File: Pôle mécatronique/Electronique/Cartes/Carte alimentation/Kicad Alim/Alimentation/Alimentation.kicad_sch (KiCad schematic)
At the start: 16 parts, among them J1 Conn_01x04, J2 Conn_01x04, J3 Conn_01x04, J4 Conn_01x05, J5 Conn_01x05, J6 Conn_02x03_Odd_Even, J7 Conn_02x10_Odd_Even, J8 Conn_01x02, J9 Conn_01x02, K1 G5LE-1, Q1 BD135, U1 TSR_2-2450, U2 TSR_2-2450, U3 TSR_2-24120

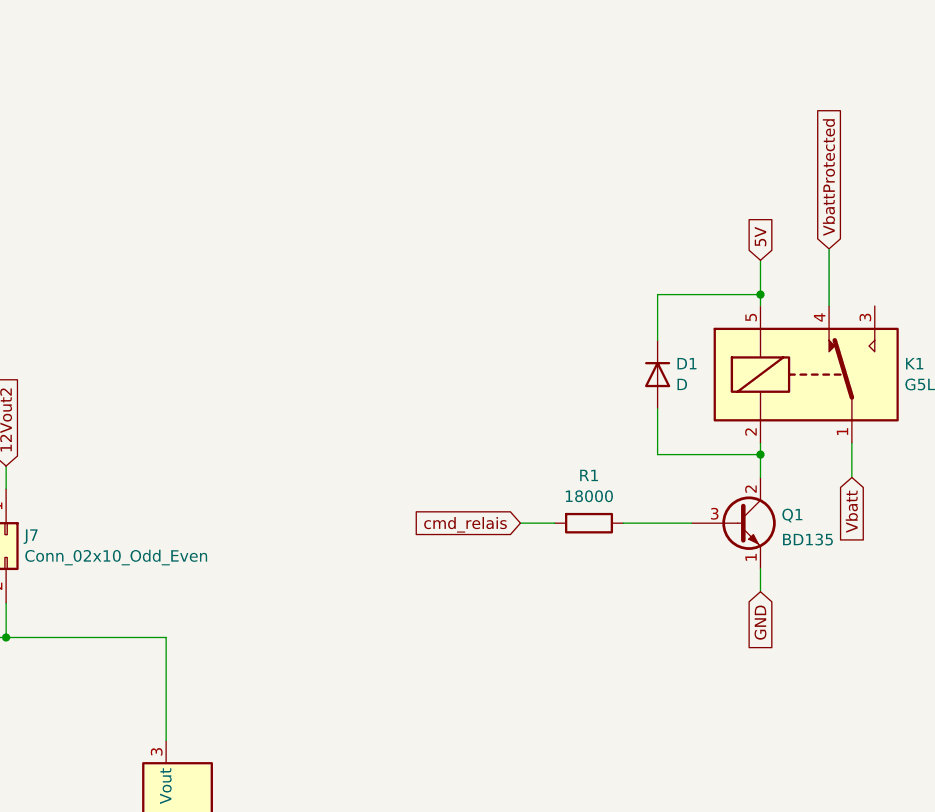
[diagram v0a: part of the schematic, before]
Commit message: Update Alim
Transistor alimenté en 12V
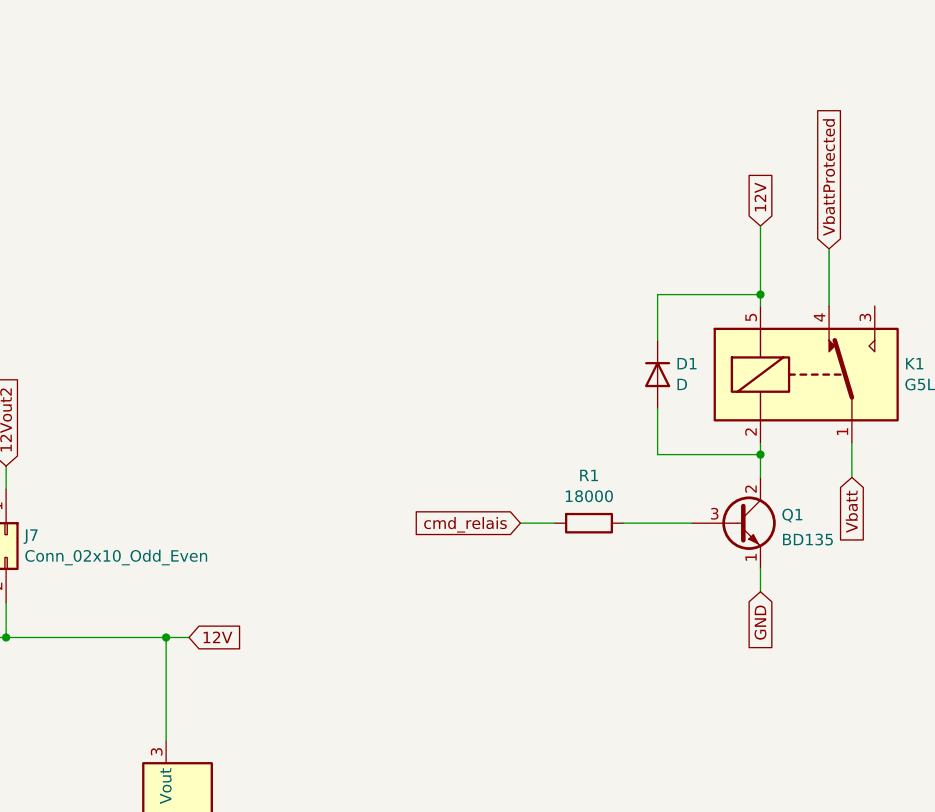
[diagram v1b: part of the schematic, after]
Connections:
- net 5V: no longer D1.1 (K), K1.5
- net 12V: now reaches J7.2 (Pin_2), J7.4 (Pin_4), U3.3 (Vout)
- net 12V: now also D1.1 (K), K1.5
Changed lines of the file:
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@@
   (junction (at 72.39 176.53) (diameter 0) (color 0 0 0 0)
   )
+  (junction (at 124.46 133.35) (diameter 0) (color 0 0 0 0)
+  )
   (junction (at 93.98 142.24) (diameter 0) (color 0 0 0 0)
   )
@@
     (stroke (width 0) (type default) (color 0 0 0 0))
   )
+  (wire (pts (xy 190.5 87.63) (xy 190.5 95.25))
+    (stroke (width 0) (type default) (color 0 0 0 0))
+  )
   (wire (pts (xy 85.09 30.48) (xy 85.09 33.02))
     (stroke (width 0) (type default) (color 0 0 0 0))
@@
     (stroke (width 0) (type default) (color 0 0 0 0))
   )
+  (wire (pts (xy 124.46 133.35) (xy 127 133.35))
+    (stroke (width 0) (type default) (color 0 0 0 0))
+  )
   (wire (pts (xy 99.06 142.24) (xy 93.98 142.24))
     (stroke (width 0) (type default) (color 0 0 0 0))
@@
     (stroke (width 0) (type default) (color 0 0 0 0))
   )
-  (wire (pts (xy 190.5 91.44) (xy 190.5 95.25))
-    (stroke (width 0) (type default) (color 0 0 0 0))
-  )
   (wire (pts (xy 91.44 133.35) (xy 93.98 133.35))
     (stroke (width 0) (type default) (color 0 0 0 0))
@@
     )
   )
+  (global_label "12V" (shape input) (at 127 133.35 0) (fields_autoplaced)
+    (effects (font (size 1.27 1.27)) (justify left))
+    (property "Intersheet References" "${INTERSHEET_REFS}" (id 0) (at 132.8318 133.2706 0)
+      (effects (font (size 1.27 1.27)) (justify left) hide)
+    )
+  )
+  (global_label "12V" (shape input) (at 190.5 87.63 90) (fields_autoplaced)
+    (effects (font (size 1.27 1.27)) (justify left))
+    (property "Intersheet References" "${INTERSHEET_REFS}" (id 0) (at 190.4206 81.7982 90)
+      (effects (font (size 1.27 1.27)) (justify left) hide)
+    )
+  )
   (global_label "can_L" (shape input) (at 82.55 33.02 270) (fields_autoplaced)
     (effects (font (size 1.27 1.27)) (justify right))
@@
     (property "Intersheet References" "${INTERSHEET_REFS}" (id 0) (at 0 0 0)
       (effects (font (size 1.27 1.27)) hide)
-    )
-  )
-  (global_label "5V" (shape input) (at 190.5 91.44 90) (fields_autoplaced)
-    (effects (font (size 1.27 1.27)) (justify left))
-    (property "Intersheet References" "${INTERSHEET_REFS}" (id 0) (at 0 0 0)
-      (effects (font (size 1.27 1.27)) hide)

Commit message: Update alim sécurité
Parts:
- added F1, F2, F3: 2A, Fuse:Fuse_BelFuse_0ZRE0012FF_L8.3mm_W3.8mm, symbol Device:Fuse
- added SW1: SW_DPDT_x2, Autre:Switch_3_Pin, symbol Switch:SW_DPDT_x2
- J8: value Conn_01x02 -> 24V in
- J9: value Conn_01x02 -> 24V out
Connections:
- net Vbatt: now also F1.2, F2.2; no longer J9.2 (Pin_2), U1.1 (Vin), U2.1 (Vin)
- net at K1.3: now also SW1.1 (A)
- net VbattProtected: no longer names the net of U3.1 (Vin)
- net VbattProtected: now also F3.1; no longer K1.4
- new net: F2.1, U2.1 (Vin)
- new net: F1.1, U1.1 (Vin)
- new net: K1.4, SW1.3 (C)
- new net VbattRelay: F3.2, J9.2 (Pin_2), SW1.2 (B)
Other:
- note added: "Commande relais de coupure du rail 24V"
- moved on the sheet: D1, J8, J9, K1, Q1, R1

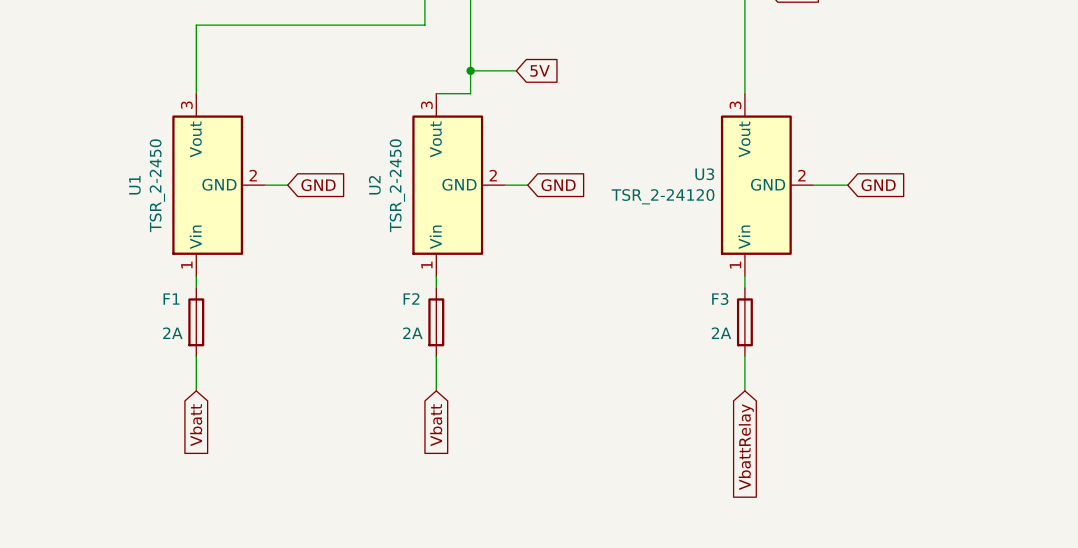
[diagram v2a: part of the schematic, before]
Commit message: Update Alim
Fusible
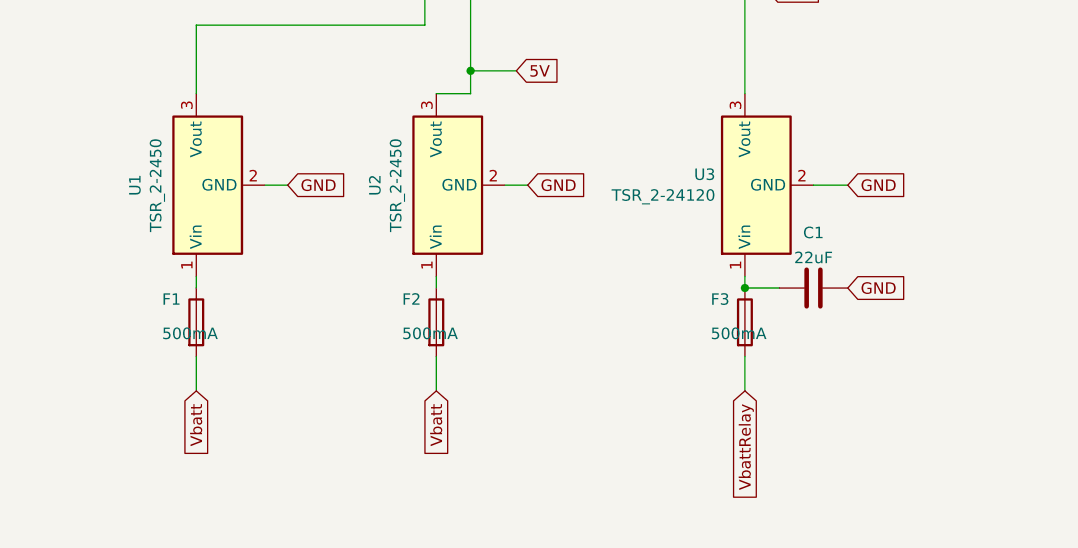
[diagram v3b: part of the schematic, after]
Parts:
- added C1: 22uF, Capacitor_THT:CP_Radial_D5.0mm_P2.00mm, symbol Device:C
- F1, F2, F3: value 2A -> 500mA
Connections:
- net GND: now also C1.2
- net at F3.1, U3.1 (Vin): now also C1.1
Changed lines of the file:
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@@
   (junction (at 124.46 133.35) (diameter 0) (color 0 0 0 0)
   )
+  (junction (at 124.46 166.37) (diameter 0) (color 0 0 0 0)
+  )
   (junction (at 93.98 142.24) (diameter 0) (color 0 0 0 0)
   )
@@
   )
   (wire (pts (xy 25.4 66.04) (xy 29.21 66.04))
+    (stroke (width 0) (type default) (color 0 0 0 0))
+  )
+  (wire (pts (xy 124.46 166.37) (xy 128.27 166.37))
     (stroke (width 0) (type default) (color 0 0 0 0))
   )
@@
     (effects (font (size 1.27 1.27)) (justify right))
     (property "Intersheet References" "${INTERSHEET_REFS}" (id 0) (at 0 0 0)
+      (effects (font (size 1.27 1.27)) hide)
+    )
+  )
+  (global_label "GND" (shape input) (at 135.89 166.37 0) (fields_autoplaced)
+    (effects (font (size 1.27 1.27)) (justify left))
+    (property "Intersheet References" "${INTERSHEET_REFS}" (id 0) (at 0 11.43 0)
       (effects (font (size 1.27 1.27)) hide)
     )
@@
     (pin "5")
   )
+  (symbol (lib_id "Device:C") (at 132.08 166.37 90) (unit 1)
+    (in_bom yes) (on_board yes) (fields_autoplaced)
+    (property "Reference" "C1" (id 0) (at 132.08 160.2445 90))
+    (property "Value" "22uF" (id 1) (at 132.08 163.0196 90))
+    (property "Footprint" "Capacitor_THT:CP_Radial_D5.0mm_P2.00mm" (id 2) (at 135.89 165.4048 0)
+      (effects (font (size 1.27 1.27)) hide)
+    )
+    (property "Datasheet" "~" (id 3) (at 132.08 166.37 0)
+      (effects (font (size 1.27 1.27)) hide)
+    )
+    (pin "1")
+    (pin "2")
+  )
   (symbol (lib_id "Switch:SW_DPDT_x2") (at 242.57 72.39 270) (unit 1)
     (in_bom yes) (on_board yes) (fields_autoplaced)
@@
       (effects (font (size 1.27 1.27)) (justify left))
     )
-    (property "Value" "2A" (id 1) (at 120.65 171.45 0)
+    (property "Value" "500mA" (id 1) (at 120.65 171.45 0)
       (effects (font (size 1.27 1.27)) (justify left))
     )
@@
       (effects (font (size 1.27 1.27)) (justify left))
     )
-    (property "Value" "2A" (id 1) (at 86.36 171.45 0)
+    (property "Value" "500mA" (id 1) (at 86.36 171.45 0)
       (effects (font (size 1.27 1.27)) (justify left))
     )
@@
       (effects (font (size 1.27 1.27)) (justify left))
     )
-    (property "Value" "2A" (id 1) (at 59.69 171.45 0)
+    (property "Value" "500mA" (id 1) (at 59.69 171.45 0)
       (effects (font (size 1.27 1.27)) (justify left))
     )
@@
   )
   (symbol_instances
+    (path "/64bbd1a8-b20b-4d12-891d-7b53b4a0334a"
+      (reference "C1") (unit 1) (value "22uF") (footprint "Capacitor_THT:CP_Radial_D5.0mm_P2.00mm")
+    )
     (path "/00000000-0000-0000-0000-000061bf5af4"
       (reference "D1") (unit 1) (value "D") (footprint "Diode_THT:D_DO-15_P12.70mm_Horizontal")
     )
     (path "/efa64a4d-4760-4db8-9b5c-8dec3e990122"
-      (reference "F1") (unit 1) (value "2A") (footprint "Fuse:Fuse_BelFuse_0ZRE0012FF_L8.3mm_W3.8mm")
+      (reference "F1") (unit 1) (value "500mA") (footprint "Fuse:Fuse_BelFuse_0ZRE0012FF_L8.3mm_W3.8mm")
     )
     (path "/dcabcaeb-fe09-4ac8-b57e-369c9887a6f6"
-      (reference "F2") (unit 1) (value "2A") (footprint "Fuse:Fuse_BelFuse_0ZRE0012FF_L8.3mm_W3.8mm")
+      (reference "F2") (unit 1) (value "500mA") (footprint "Fuse:Fuse_BelFuse_0ZRE0012FF_L8.3mm_W3.8mm")
     )
     (path "/b4241bca-1ea3-4639-887d-87554bfe24e4"
-      (reference "F3") (unit 1) (value "2A") (footprint "Fuse:Fuse_BelFuse_0ZRE0012FF_L8.3mm_W3.8mm")
+      (reference "F3") (unit 1) (value "500mA") (footprint "Fuse:Fuse_BelFuse_0ZRE0012FF_L8.3mm_W3.8mm")
     )
     (path "/00000000-0000-0000-0000-000061a9c7ae"

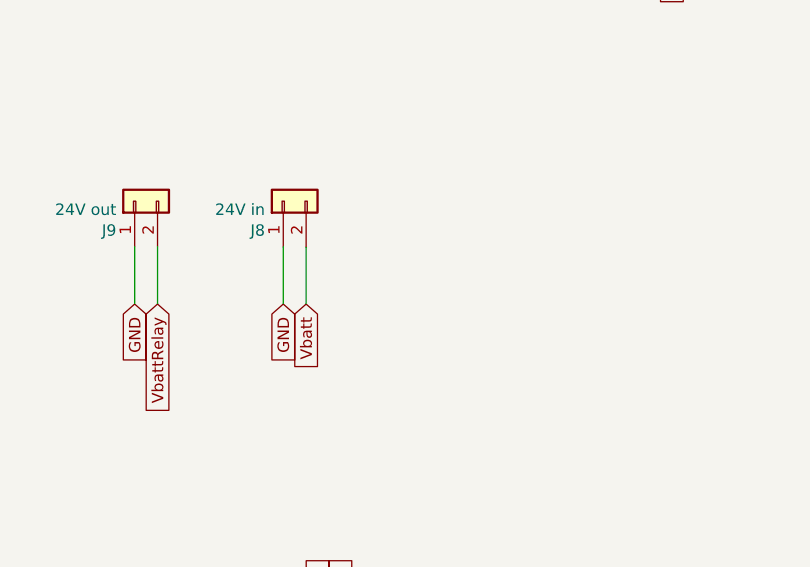
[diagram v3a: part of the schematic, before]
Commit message: Update alim
- Ajout de la connexion du bus can à la BR
- Normalisation des perçages
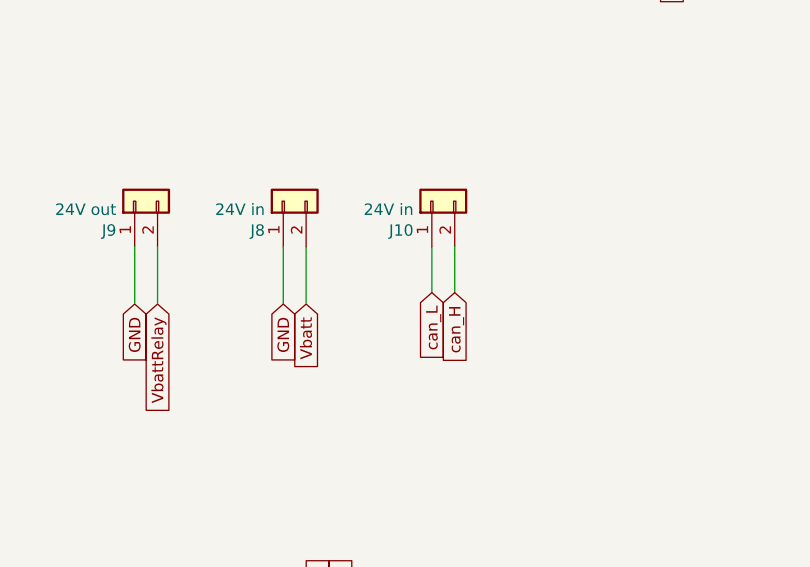
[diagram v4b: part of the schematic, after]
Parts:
- added J10: 24V in, Connector_JST:JST_PH_B2B-PH-K_1x02_P2.00mm_Vertical, symbol Connector_Generic:Conn_01x02
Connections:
- net can_H: now also J10.2 (Pin_2)
- net can_L: now also J10.1 (Pin_1)
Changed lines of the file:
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@@
+    (stroke (width 0) (type default) (color 0 0 0 0))
+  )
+  (wire (pts (xy 119.38 69.85) (xy 119.38 74.93))
     (stroke (width 0) (type default) (color 0 0 0 0))
   )
@@
   )
   (wire (pts (xy 99.06 133.35) (xy 101.6 133.35))
+    (stroke (width 0) (type default) (color 0 0 0 0))
+  )
+  (wire (pts (xy 116.84 69.85) (xy 116.84 74.93))
     (stroke (width 0) (type default) (color 0 0 0 0))
   )
@@
     )
   )
+  (global_label "can_L" (shape input) (at 116.84 74.93 270) (fields_autoplaced)
+    (effects (font (size 1.27 1.27)) (justify right))
+    (property "Intersheet References" "${INTERSHEET_REFS}" (id 0) (at -48.26 41.91 0)
+      (effects (font (size 1.27 1.27)) hide)
+    )
+  )
   (global_label "can_H" (shape input) (at 80.01 33.02 270) (fields_autoplaced)
     (effects (font (size 1.27 1.27)) (justify right))
@@
     (effects (font (size 1.27 1.27)) (justify right))
     (property "Intersheet References" "${INTERSHEET_REFS}" (id 0) (at 0 0 0)
+      (effects (font (size 1.27 1.27)) hide)
+    )
+  )
+  (global_label "can_H" (shape input) (at 119.38 74.93 270) (fields_autoplaced)
+    (effects (font (size 1.27 1.27)) (justify right))
+    (property "Intersheet References" "${INTERSHEET_REFS}" (id 0) (at -43.18 41.91 0)
       (effects (font (size 1.27 1.27)) hide)
     )
@@
     (pin "5")
   )
+  (symbol (lib_id "Connector_Generic:Conn_01x02") (at 116.84 64.77 90) (unit 1)
+    (in_bom yes) (on_board yes)
+    (property "Reference" "J10" (id 0) (at 114.808 68.0212 90)
+      (effects (font (size 1.27 1.27)) (justify left))
+    )
+    (property "Value" "24V in" (id 1) (at 114.808 65.7098 90)
+      (effects (font (size 1.27 1.27)) (justify left))
+    )
+    (property "Footprint" "Connector_JST:JST_PH_B2B-PH-K_1x02_P2.00mm_Vertical" (id 2) (at 116.84 64.77 0)
+      (effects (font (size 1.27 1.27)) hide)
+    )
+    (property "Datasheet" "~" (id 3) (at 116.84 64.77 0)
+      (effects (font (size 1.27 1.27)) hide)
+    )
+    (pin "1")
+    (pin "2")
+  )
   (symbol (lib_id "Device:C") (at 132.08 166.37 90) (unit 1)
     (in_bom yes) (on_board yes) (fields_autoplaced)
@@
       (reference "J9") (unit 1) (value "24V out") (footprint "Connector_AMASS:AMASS_XT60-F_1x02_P7.20mm_Vertical")
     )
+    (path "/1e9dcbc0-ed04-41e3-9512-fbb37cd7d179"
+      (reference "J10") (unit 1) (value "24V in") (footprint "Connector_JST:JST_PH_B2B-PH-K_1x02_P2.00mm_Vertical")
+    )
     (path "/00000000-0000-0000-0000-000061aee719"

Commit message: Correction pcb BR
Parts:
- added R2, R3: 120, Resistor_THT:R_Axial_DIN0207_L6.3mm_D2.5mm_P10.16mm_Horizontal, symbol Device:R
- added TP1, TP2, TP3, TP4, TP5, TP6, TP7, TP8, TP9: TestPoint, TestPoint:TestPoint_Pad_D2.0mm, symbol Connector:TestPoint
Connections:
- net 12V: now also TP4.1
- net Vbatt: now also TP6.1; no longer F2.2
- net VbattRelay: now also F2.2
- net can_H: now also R2.1, R3.1, TP2.1
- net can_L: now also R2.2, R3.2, TP1.1
- net cmd_relais: now also TP8.1
- net at D1.2 (A), K1.2, Q1.2 (C): now also TP3.1
- net at K1.3, SW1.1 (A): now also TP7.1
- net at K1.4, SW1.3 (C): now also TP5.1
- net at Q1.3 (B), R1.1: now also TP9.1

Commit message: Minor changes
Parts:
- R1: value 18000 -> 1600
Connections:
- net 12V: no longer D1.1 (K), K1.5, TP4.1
- net 5VRPI: now also D1.1 (K), K1.5, TP4.1
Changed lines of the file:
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@@
     (stroke (width 0) (type default) (color 0 0 0 0))
   )
-  (wire (pts (xy 232.41 71.12) (xy 232.41 76.2))
+  (wire (pts (xy 232.41 68.58) (xy 232.41 76.2))
     (stroke (width 0) (type default) (color 0 0 0 0))
   )
@@
     )
   )
+  (global_label "5VRPI" (shape input) (at 232.41 68.58 90) (fields_autoplaced)
+    (effects (font (size 1.27 1.27)) (justify left))
+    (property "Intersheet References" "${INTERSHEET_REFS}" (id 0) (at 143.51 -45.72 0)
+      (effects (font (size 1.27 1.27)) hide)
+    )
+  )
   (global_label "12V" (shape input) (at 127 133.35 0) (fields_autoplaced)
     (effects (font (size 1.27 1.27)) (justify left))
     (property "Intersheet References" "${INTERSHEET_REFS}" (id 0) (at 132.8318 133.2706 0)
-      (effects (font (size 1.27 1.27)) (justify left) hide)
-    )
-  )
-  (global_label "12V" (shape input) (at 232.41 71.12 90) (fields_autoplaced)
-    (effects (font (size 1.27 1.27)) (justify left))
-    (property "Intersheet References" "${INTERSHEET_REFS}" (id 0) (at 232.3306 65.2882 90)
       (effects (font (size 1.27 1.27)) (justify left) hide)
     )
@@
     (in_bom yes) (on_board yes)
     (property "Reference" "R1" (id 0) (at 213.36 98.8822 90))
-    (property "Value" "18000" (id 1) (at 213.36 101.1936 90))
+    (property "Value" "1600" (id 1) (at 213.36 101.1936 90))
     (property "Footprint" "Resistor_THT:R_Axial_DIN0207_L6.3mm_D2.5mm_P10.16mm_Horizontal" (id 2) (at 213.36 102.362 90)
       (effects (font (size 1.27 1.27)) hide)
@@
     )
     (path "/00000000-0000-0000-0000-000061b93dbb"
-      (reference "R1") (unit 1) (value "18000") (footprint "Resistor_THT:R_Axial_DIN0207_L6.3mm_D2.5mm_P10.16mm_Horizontal")
+      (reference "R1") (unit 1) (value "1600") (footprint "Resistor_THT:R_Axial_DIN0207_L6.3mm_D2.5mm_P10.16mm_Horizontal")
     )
     (path "/c4c5a52a-59bb-4103-b05b-78908e6fcd3d"
